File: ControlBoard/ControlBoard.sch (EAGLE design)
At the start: 7 parts, among them J1 FTDI_DEVICE

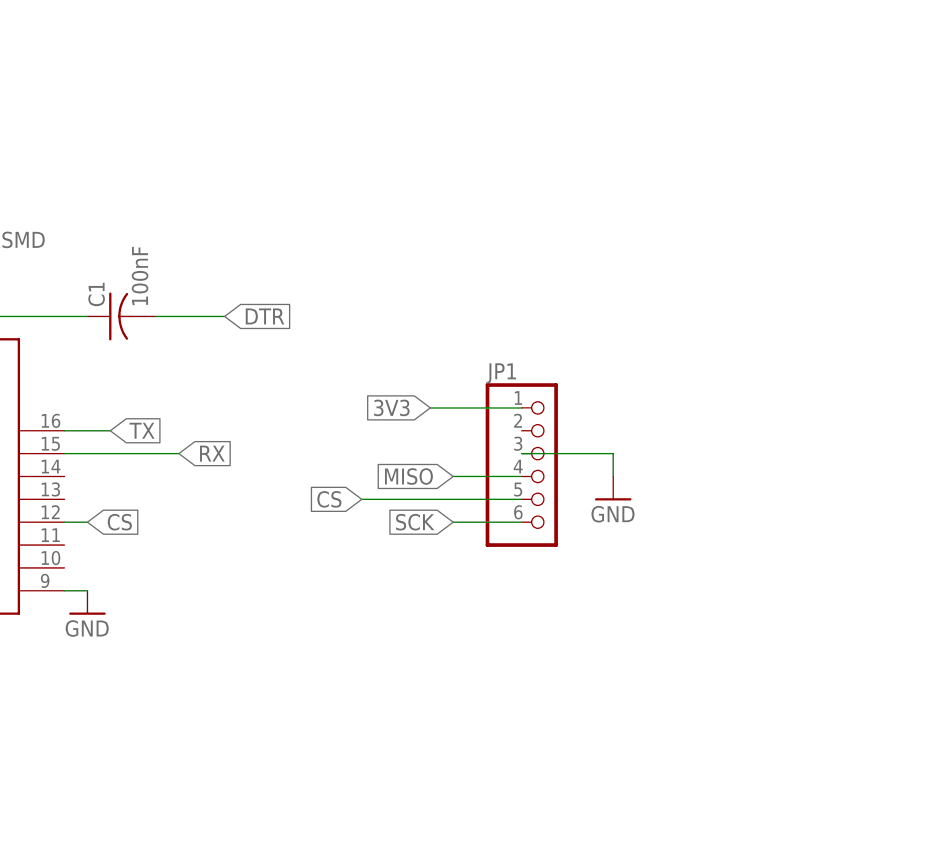
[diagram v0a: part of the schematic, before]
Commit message: added thermocouple-digital chip
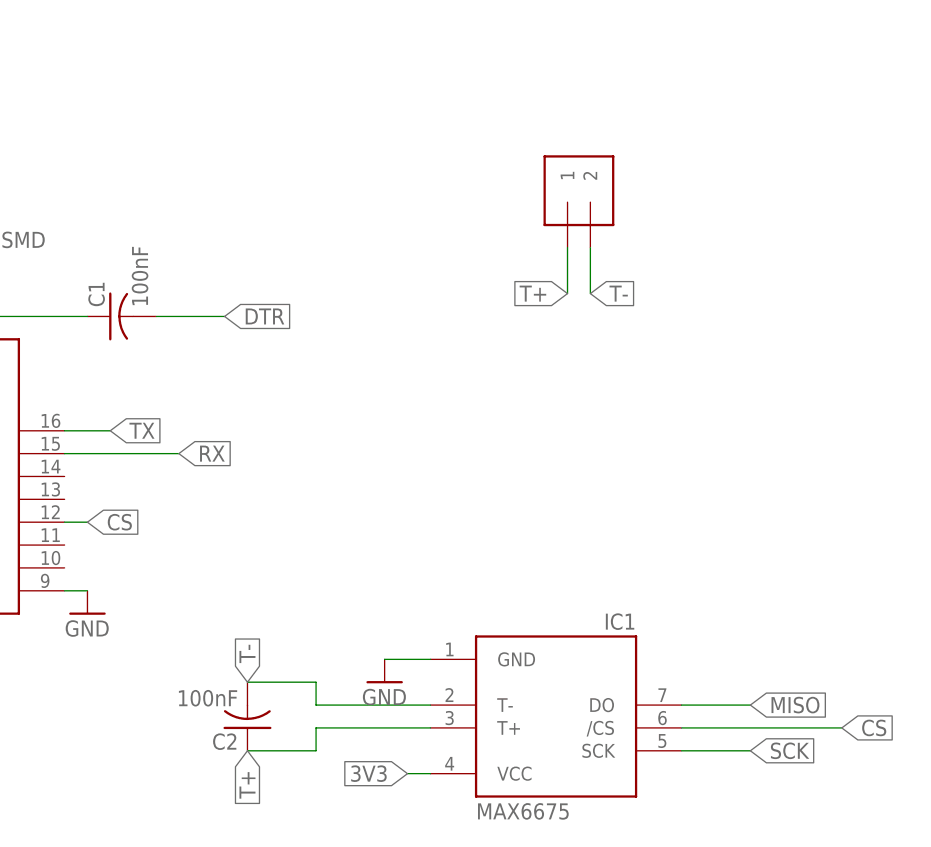
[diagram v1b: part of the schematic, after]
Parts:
- removed JP1: (no value), adafruit:PINHD-1X6
- added C2: 100nF, rcl:C-USC0603
- added IC1: MAX6675, adafruit:MAX6675
- added J2: 1X2-3.5MM, adafruit:1X2-3.5MM
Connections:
- new net T+: C2.1, IC1.T+, J2.1
- new net T-: C2.2, IC1.T-, J2.2
- net 3V3: now also IC1.VCC; no longer JP1.1
- net CS: now also IC1./CS; no longer JP1.5
- net GND: now also IC1.GND; no longer JP1.3
- net MISO: now also IC1.DO; no longer JP1.4
- net SCK: now also IC1.SCK; no longer JP1.6
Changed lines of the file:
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@@
 <parts>
 <part name="X1" library="adafruit" deviceset="ESP-12" device=""/>
-<part name="JP1" library="adafruit" deviceset="PINHD-1X6" device=""/>
 <part name="GND1" library="supply1" deviceset="GND" device=""/>
 <part name="GND2" library="supply1" deviceset="GND" device=""/>
@@
 <part name="GND3" library="supply1" deviceset="GND" device=""/>
 <part name="C1" library="rcl" deviceset="C-US" device="C0603" value="100nF"/>
+<part name="IC1" library="adafruit" deviceset="MAX6675" device=""/>
+<part name="C2" library="rcl" deviceset="C-US" device="C0603" value="100nF"/>
+<part name="J2" library="adafruit" deviceset="1X2" device="-3.5MM"/>
 </parts>
 <sheets>
@@
 <instances>
 <instance part="X1" gate="G$1" x="5.08" y="53.34"/>
-<instance part="JP1" gate="A" x="76.2" y="53.34"/>
 <instance part="GND1" gate="1" x="25.4" y="38.1"/>
-<instance part="GND2" gate="1" x="83.82" y="50.8"/>
+<instance part="GND2" gate="1" x="58.42" y="30.48"/>
 <instance part="J1" gate="G$1" x="-58.42" y="86.36" rot="R90"/>
 <instance part="R1" gate="G$1" x="-25.4" y="53.34"/>
@@
 <instance part="GND3" gate="1" x="-2.54" y="76.2"/>
 <instance part="C1" gate="G$1" x="27.94" y="71.12" rot="R90"/>
+<instance part="IC1" gate="G$1" x="76.2" y="30.48"/>
+<instance part="C2" gate="G$1" x="43.18" y="25.4" rot="R180"/>
+<instance part="J2" gate="G$1" x="81.28" y="83.82" rot="R90"/>
 </instances>
 <busses>
@@
 </segment>
 <segment>
-<pinref part="JP1" gate="A" pin="3"/>
-<wire x1="73.66" y1="55.88" x2="83.82" y2="55.88" width="0.1524" layer="91"/>
-<wire x1="83.82" y1="55.88" x2="83.82" y2="53.34" width="0.1524" layer="91"/>
-<pinref part="GND2" gate="1" pin="GND"/>
-</segment>
-<segment>
 <pinref part="S1" gate="G$1" pin="2"/>
 <pinref part="GND3" gate="1" pin="GND"/>
 <wire x1="-2.54" y1="78.74" x2="-2.54" y2="81.28" width="0.1524" layer="91"/>
 </segment>
+<segment>
+<pinref part="GND2" gate="1" pin="GND"/>
+<pinref part="IC1" gate="G$1" pin="GND"/>
+<wire x1="58.42" y1="33.02" x2="63.5" y2="33.02" width="0.1524" layer="91"/>
+</segment>
 </net>
 <net name="SCK" class="0">
@@
 </segment>
 <segment>
-<pinref part="JP1" gate="A" pin="6"/>
-<wire x1="73.66" y1="48.26" x2="66.04" y2="48.26" width="0.1524" layer="91"/>
-<label x="66.04" y="48.26" size="1.778" layer="95" rot="R180" xref="yes"/>
+<pinref part="IC1" gate="G$1" pin="SCK"/>
+<wire x1="91.44" y1="22.86" x2="99.06" y2="22.86" width="0.1524" layer="91"/>
+<label x="99.06" y="22.86" size="1.778" layer="95" xref="yes"/>
 </segment>
 </net>
@@
 </segment>
 <segment>
-<pinref part="JP1" gate="A" pin="4"/>
-<wire x1="73.66" y1="53.34" x2="66.04" y2="53.34" width="0.1524" layer="91"/>
-<label x="66.04" y="53.34" size="1.778" layer="95" rot="R180" xref="yes"/>
+<pinref part="IC1" gate="G$1" pin="DO"/>
+<wire x1="99.06" y1="27.94" x2="91.44" y2="27.94" width="0.1524" layer="91"/>
+<label x="99.06" y="27.94" size="1.778" layer="95" xref="yes"/>
 </segment>
 </net>
@@
 </segment>
 <segment>
-<pinref part="JP1" gate="A" pin="5"/>
-<wire x1="73.66" y1="50.8" x2="55.88" y2="50.8" width="0.1524" layer="91"/>
-<label x="55.88" y="50.8" size="1.778" layer="95" rot="R180" xref="yes"/>
+<pinref part="IC1" gate="G$1" pin="/CS"/>
+<wire x1="91.44" y1="25.4" x2="109.22" y2="25.4" width="0.1524" layer="91"/>
+<label x="109.22" y="25.4" size="1.778" layer="95" xref="yes"/>
 </segment>
 </net>
@@
 </segment>
 <segment>
-<pinref part="JP1" gate="A" pin="1"/>
-<wire x1="73.66" y1="60.96" x2="63.5" y2="60.96" width="0.1524" layer="91"/>
-<label x="63.5" y="60.96" size="1.778" layer="95" rot="R180" xref="yes"/>
+<label x="60.96" y="20.32" size="1.778" layer="95" rot="R180" xref="yes"/>
+<pinref part="IC1" gate="G$1" pin="VCC"/>
+<wire x1="63.5" y1="20.32" x2="60.96" y2="20.32" width="0.1524" layer="91"/>
 </segment>
 <segment>
@@
 </segment>
 </net>
+<net name="T-" class="0">
+<segment>
+<pinref part="C2" gate="G$1" pin="2"/>
+<wire x1="43.18" y1="30.48" x2="50.8" y2="30.48" width="0.1524" layer="91"/>
+<wire x1="50.8" y1="30.48" x2="50.8" y2="27.94" width="0.1524" layer="91"/>
+<pinref part="IC1" gate="G$1" pin="T-"/>
+<wire x1="50.8" y1="27.94" x2="63.5" y2="27.94" width="0.1524" layer="91"/>
+<label x="43.18" y="30.48" size="1.778" layer="95" rot="R90" xref="yes"/>
+</segment>
+<segment>
+<pinref part="J2" gate="G$1" pin="2"/>
+<wire x1="81.28" y1="78.74" x2="81.28" y2="73.66" width="0.1524" layer="91"/>
+<label x="81.28" y="73.66" size="1.778" layer="95" xref="yes"/>
+</segment>
+</net>
+<net name="T+" class="0">
+<segment>
+<pinref part="IC1" gate="G$1" pin="T+"/>
+<wire x1="63.5" y1="25.4" x2="50.8" y2="25.4" width="0.1524" layer="91"/>
+<wire x1="50.8" y1="25.4" x2="50.8" y2="22.86" width="0.1524" layer="91"/>
+<pinref part="C2" gate="G$1" pin="1"/>
+<wire x1="50.8" y1="22.86" x2="43.18" y2="22.86" width="0.1524" layer="91"/>
+<label x="43.18" y="22.86" size="1.778" layer="95" rot="R270" xref="yes"/>
+</segment>
+<segment>
+<pinref part="J2" gate="G$1" pin="1"/>
+<wire x1="78.74" y1="78.74" x2="78.74" y2="73.66" width="0.1524" layer="91"/>
+<label x="78.74" y="73.66" size="1.778" layer="95" rot="R180" xref="yes"/>
+</segment>
+</net>

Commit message: updated eagle board and schematic files
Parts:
- added C3, C4: 1uF, rcl:C-USC0603
- added J3: 1X2-3.5MM, adafruit:1X2-3.5MM
- added MCP1802T-3302I/OT: MCP1802T-3002I/OT, quad:MCP1802T-3002I/OT
- added T1: 2N4401, transistor:-NPN-TO92-EBC
- added X2: MINI-USB-32005-201, con-cypressindustries:MINI-USB-32005-201
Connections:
- net T+ renamed THERMOCOUPLE+
- net T- renamed THERMOCOUPLE-
- removed net N$1: J1.CTS, J1.GND
- new net 5V: C3.1, MCP1802T-3302I/OT.VIN, MCP1802T-3302I/OT.~SHDN, T1.C, X2.1
- new net CTS: J1.CTS, X1.GPIO13
- new net RELAY_COIL: J3.1, T1.E
- new net RELAY_CTRL: T1.B, X1.GPIO4
- net 3V3: now also C4.1, MCP1802T-3302I/OT.VOUT
- net CS: now also X1.GPIO15; no longer X1.GPIO0
- net GND: now also C3.2, C4.2, J1.GND, J3.2, MCP1802T-3302I/OT.VSS, X2.5
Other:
- moved on the sheet: C2, IC1
